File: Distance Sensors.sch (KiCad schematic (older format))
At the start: 6 parts, among them U5 VL53L0X, U6 VL53L0X, U7 VL53L0X

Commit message: Major upgrade
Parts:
- removed R11, R12, R13: 47K, Resistor_SMD:R_0402_1005Metric, symbol Device:R_Small
- removed U5, U6, U7: VL53L0X, synermycha-electronics:SENSOR_VL53L0X, symbol VL53L0X:VL53L0X
- added J12, J13, J14, J15, J16: Conn_01x05, connector_brd2brd:01x05_1.0x0.5mm_SMD, symbol Connector_Generic:Conn_01x05
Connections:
- net labels added: VL53L0x_~XSHUT[4], VL53L0x_~XSHUT[5]
- wire segments 59 -> 37

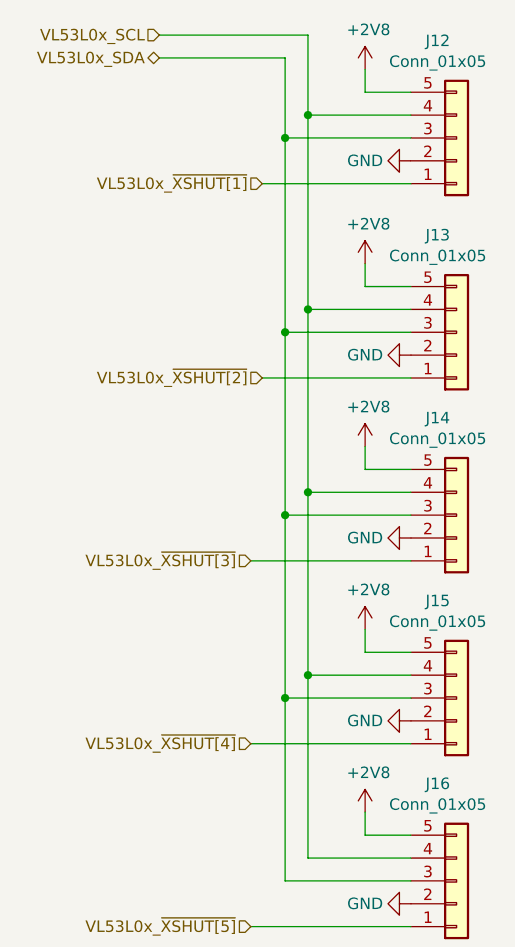
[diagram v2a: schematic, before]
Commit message: Czyszczenie
Usunięto linie 5V oraz 2V8. Poprawiono symbol dla diody RGB
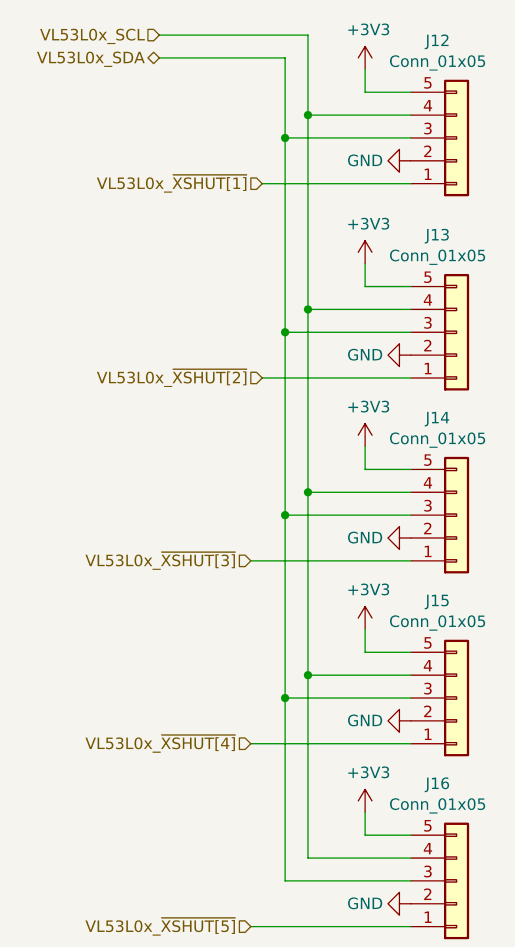
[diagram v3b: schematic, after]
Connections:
- net +2V8 renamed +3V3
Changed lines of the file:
@@
-$EndComp
-$Comp
-L power:+2V8 #PWR0210
-U 1 1 5E6B084C
-P 7250 1500
-F 0 "#PWR0210" H 7250 1350 50  0001 C CNN
-F 1 "+2V8" H 7265 1673 50  0000 C CNN
-F 2 "" H 7250 1500 50  0001 C CNN
-F 3 "" H 7250 1500 50  0001 C CNN
-	1    7250 1500
-	1    0    0    -1
 $EndComp
 $Comp
@@
 	7250 1600 7250 1500
 $Comp
-L power:+2V8 #PWR0212
-U 1 1 5E6B8F53
-P 7250 2350
-F 0 "#PWR0212" H 7250 2200 50  0001 C CNN
-F 1 "+2V8" H 7265 2523 50  0000 C CNN
-F 2 "" H 7250 2350 50  0001 C CNN
-F 3 "" H 7250 2350 50  0001 C CNN
-	1    7250 2350
-	1    0    0    -1
-$EndComp
-$Comp
 L power:GND #PWR0213
 U 1 1 5E6B8F59
@@
 Wire Wire Line
 	7450 2450 7250 2450
-Wire Wire Line
-	7250 2450 7250 2350
-$Comp
-L power:+2V8 #PWR0214
-U 1 1 5E6BC2E7
-P 7250 3150
-F 0 "#PWR0214" H 7250 3000 50  0001 C CNN
-F 1 "+2V8" H 7265 3323 50  0000 C CNN
-F 2 "" H 7250 3150 50  0001 C CNN
-F 3 "" H 7250 3150 50  0001 C CNN
-	1    7250 3150
-	1    0    0    -1
-$EndComp
 $Comp
 L power:GND #PWR0215
@@
 $EndComp
 $Comp
-L power:+2V8 #PWR0132
-U 1 1 5E62698C
-P 7250 3950
-F 0 "#PWR0132" H 7250 3800 50  0001 C CNN
-F 1 "+2V8" H 7265 4123 50  0000 C CNN
-F 2 "" H 7250 3950 50  0001 C CNN
-F 3 "" H 7250 3950 50  0001 C CNN
-	1    7250 3950
-	1    0    0    -1
-$EndComp
-$Comp
 L power:GND #PWR0133
 U 1 1 5E626992
@@
 $EndComp
 $Comp
-L power:+2V8 #PWR0204
-U 1 1 5E62836A
-P 7250 4750
-F 0 "#PWR0204" H 7250 4600 50  0001 C CNN
-F 1 "+2V8" H 7265 4923 50  0000 C CNN
-F 2 "" H 7250 4750 50  0001 C CNN
-F 3 "" H 7250 4750 50  0001 C CNN
-	1    7250 4750
-	1    0    0    -1
-$EndComp
-$Comp
 L power:GND #PWR0205
 U 1 1 5E628370
@@
 Wire Wire Line
 	7000 1350 7000 1700
+$Comp
+L power:+3V3 #PWR0109
+U 1 1 5F625C43
+P 7250 4750
+F 0 "#PWR0109" H 7250 4600 50  0001 C CNN
+F 1 "+3V3" H 7265 4923 50  0000 C CNN
+F 2 "" H 7250 4750 50  0001 C CNN
+F 3 "" H 7250 4750 50  0001 C CNN
+	1    7250 4750
+	1    0    0    -1
+$EndComp
+$Comp
+L power:+3V3 #PWR0110
+U 1 1 5F628526
+P 7250 1500
+F 0 "#PWR0110" H 7250 1350 50  0001 C CNN
+F 1 "+3V3" H 7265 1673 50  0000 C CNN
+F 2 "" H 7250 1500 50  0001 C CNN
+F 3 "" H 7250 1500 50  0001 C CNN
+	1    7250 1500
+	1    0    0    -1
+$EndComp
+Wire Wire Line
+	7250 2450 7250 2350
+$Comp
+L power:+3V3 #PWR0111
+U 1 1 5F62A809
+P 7250 3950
+F 0 "#PWR0111" H 7250 3800 50  0001 C CNN
+F 1 "+3V3" H 7265 4123 50  0000 C CNN
+F 2 "" H 7250 3950 50  0001 C CNN
+F 3 "" H 7250 3950 50  0001 C CNN
+	1    7250 3950
+	1    0    0    -1
+$EndComp
+$Comp
+L power:+3V3 #PWR0113
+U 1 1 5F62AB3C
+P 7250 3150
+F 0 "#PWR0113" H 7250 3000 50  0001 C CNN
+F 1 "+3V3" H 7265 3323 50  0000 C CNN
+F 2 "" H 7250 3150 50  0001 C CNN
+F 3 "" H 7250 3150 50  0001 C CNN
+	1    7250 3150
+	1    0    0    -1
+$EndComp
+$Comp
+L power:+3V3 #PWR0132
+U 1 1 5F62AEA5
+P 7250 2350
+F 0 "#PWR0132" H 7250 2200 50  0001 C CNN
+F 1 "+3V3" H 7265 2523 50  0000 C CNN
+F 2 "" H 7250 2350 50  0001 C CNN
+F 3 "" H 7250 2350 50  0001 C CNN
+	1    7250 2350
+	1    0    0    -1
+$EndComp
 $EndSCHEMATC
